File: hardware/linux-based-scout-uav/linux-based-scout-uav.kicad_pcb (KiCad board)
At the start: 2 copper layers, 60 x 90 mm, 39 parts, among them J1 XT60PW-M, J2 Micro_SD_Card_Det2, J3 TC2050-IDC-NL, J4 0786463001, J5 GSB1C41110SSHR, Q1 DMP3013SFV, Q2 DMP3013SFV, U1 OSD32MP157C-512M-IAA, U2 RN2903A-I_RM098, U3 M65, U4 LC76G, U5 MPU-6050, U6 AMG8833, U7 SX1272, U8 EMMC04G-W627-M06U, U9 CYPD3177-24LQ, Y1 ABS05-32.768KHZ-7-T

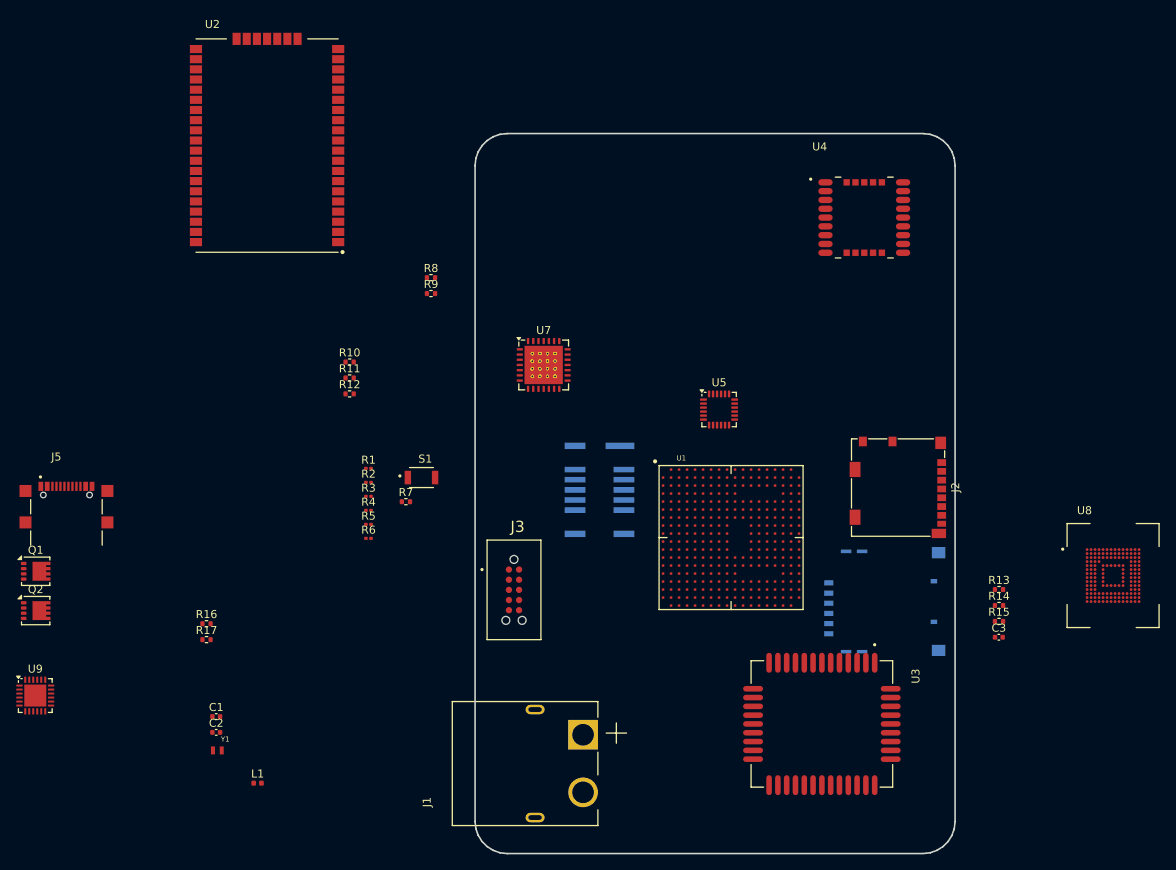
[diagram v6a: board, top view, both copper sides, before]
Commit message: Board placement update
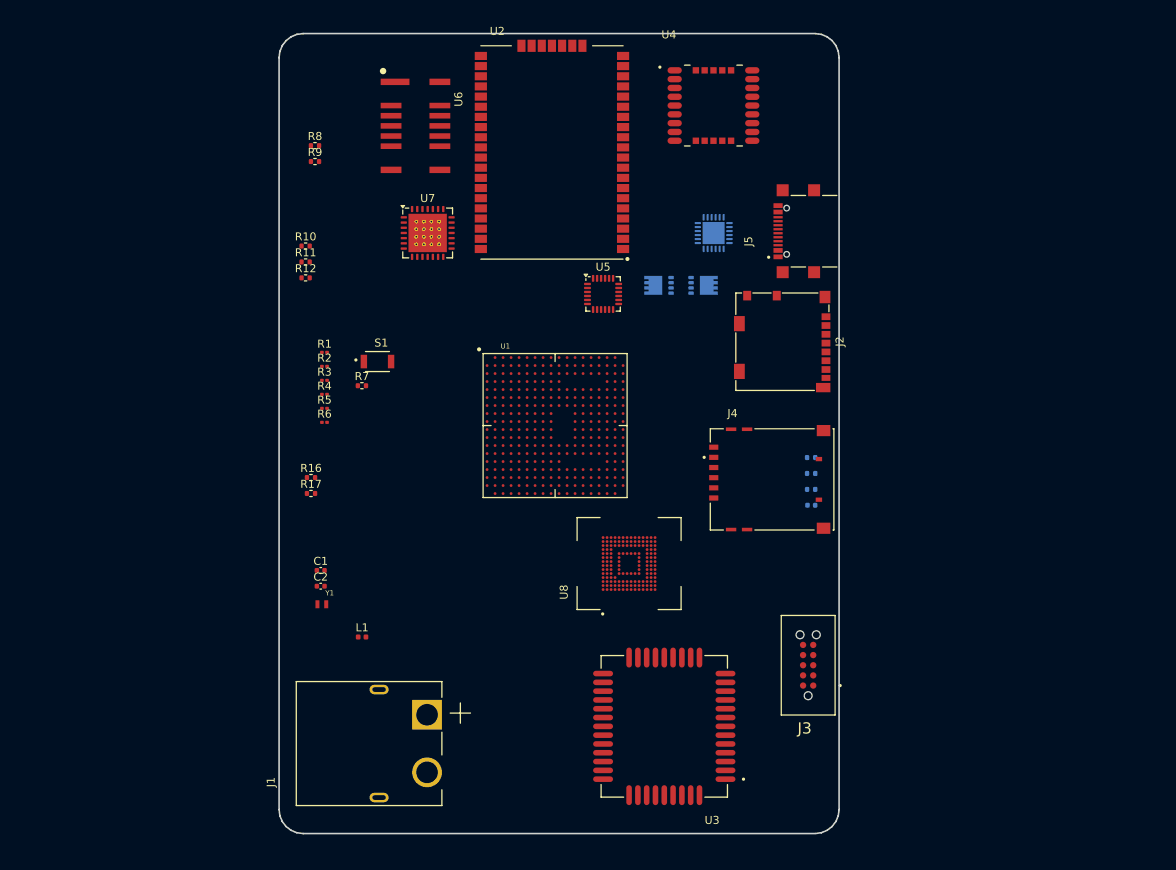
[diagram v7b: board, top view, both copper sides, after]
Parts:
- C3, Q1, Q2, R13, R14, R15, U9: moved to B.Cu
- J4, U6: moved to F.Cu
- moved U9 102.6 mm to (158.8, 74.9), turned to 180 degrees
- moved J5 99.2 mm to (170.6, 74.7), turned to 90 degrees
- moved Q1 90.8 mm to (157.5, 81.5)
- moved Q2 87.9 mm to (152.0, 81.5), turned to 180 degrees
- moved U8 60.5 mm to (148.2, 116.2), turned to 90 degrees
- moved U6 51.0 mm to (121.5, 61.5)
- moved J3 40.7 mm to (171.3, 131.5), turned to 180 degrees
- moved U2 35.6 mm to (138.6, 64.9)
- moved R13 28.7 mm to (171.0, 103.0), turned to 180 degrees
- moved R14 28.7 mm to (171.0, 105.0), turned to 180 degrees
- moved R15 28.7 mm to (171.0, 107.0), turned to 180 degrees
- moved C3 28.7 mm to (171.0, 109.0), turned to 180 degrees
- moved U1 26.1 mm to (139.0, 99.0)
- moved U4 23.5 mm to (158.8, 59.0)
- moved J2 23.3 mm to (167.4, 88.5)
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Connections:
- U1 pad D5: unconnected-(U1F-PWR_ON/PMIC_PWRCTRL-PadD5) -> Net-(U1F-PWR_ON/PMIC_PWRCTRL)
- U1 pad D6: unconnected-(U1F-PC13/PMIC_WAKEUP-PadD6) -> Net-(U1F-PC13/PMIC_WAKEUP)
- U1 pad J12: unconnected-(U1F-VTT_DDR-PadJ12) -> Net-(U1F-VTT_DDR)
- U1 pad J2: unconnected-(U1F-HSE_OSC_TP-PadJ2) -> Net-(U1F-HSE_OSC_TP)
- U1 pad K12: unconnected-(U1F-VDD_DDR-PadK12) -> Net-(U1F-VDD_DDR)
- U1 pad K6: unconnected-(U1F-PWR_LP-PadK6) -> Net-(U1F-PWR_LP)
- U1 pad L12: unconnected-(U1F-VREF_DDR-PadL12) -> Net-(U1F-VREF_DDR)
- U1 pad L3: unconnected-(U1F-PA0/PMIC_INTN-PadL3) -> Net-(U1F-PA0/PMIC_INTN)
- U1 pad L6: unconnected-(U1F-PDR_ON_CORE-PadL6) -> Net-(U1F-PDR_ON_CORE)
- U1 pad M6: unconnected-(U1F-PDR_ON-PadM6) -> Net-(U1F-PDR_ON)
- U1 pad N4: unconnected-(U1F-NRST_CORE-PadN4) -> Net-(U1F-NRST_CORE)
- U1 pad R4: unconnected-(U1F-VDD_CORE-PadR4) -> Net-(U1F-VDD_CORE)
- U1 pad R5: unconnected-(U1F-VDD3V3_USB-PadR5) -> Net-(U1F-VDD3V3_USB)
- U1 pad R6: unconnected-(U1F-VDD1V2_DSI_REG-PadR6) -> Net-(U1F-VDD1V2_DSI_REG)
- U1 pad R7: unconnected-(U1F-VDDA1V8_REG-PadR7) -> Net-(U1F-VDDA1V8_REG)
- U1 pad R8: unconnected-(U1F-VDDA1V1_REG-PadR8) -> Net-(U1F-VDDA1V1_REG)
- U1 pad T12: unconnected-(U1D-PE3-PadT12) -> MMC2_CLK
- U1 pad U15: unconnected-(U1D-PG6-PadU15) -> MMC2_CMD
- U8 pad A6: (no net) -> GND
- U8 pad A7: (no net) -> unconnected-(U8B-RFU_A7-PadA7)
- U8 pad C2: unconnected-(U8A-VDDI-PadC2) -> Net-(U8A-VDDI)
- U8 pad C4: (no net) -> GND
- U8 pad C6: (no net) -> +3V3
- U8 pad E10: GND -> unconnected-(U8A-VSF2-PadE10)
- U8 pad E5: (no net) -> unconnected-(U8B-RFU_E5-PadE5)
- U8 pad E6: (no net) -> +3V3
- U8 pad E7: (no net) -> GND
- U8 pad E8: GND -> unconnected-(U8A-VSF5-PadE8)
- U8 pad E9: GND -> unconnected-(U8A-VSF1-PadE9)
- U8 pad F10: GND -> unconnected-(U8A-VSF3-PadF10)
- U8 pad F5: (no net) -> +3V3
- U8 pad G10: GND -> unconnected-(U8A-VSF6-PadG10)
- U8 pad G3: (no net) -> unconnected-(U8B-RFU_G3-PadG3)
- U8 pad G5: (no net) -> GND
- U8 pad H1: (no net) -> Net-(U8B-NC_5-PadH1)
- U8 pad H10: (no net) -> GND
- U8 pad H12: (no net) -> Net-(U8B-NC_5-PadH1)
- U8 pad H13: (no net) -> Net-(U8B-NC_5-PadH1)
- U8 pad H14: (no net) -> Net-(U8B-NC_5-PadH1)
- U8 pad H2: (no net) -> Net-(U8B-NC_5-PadH1)
- U8 pad H3: (no net) -> Net-(U8B-NC_5-PadH1)
- U8 pad H5: unconnected-(U8A-DS-PadH5) -> Net-(U8A-DS)
- U8 pad J1: (no net) -> Net-(U8B-NC_5-PadH1)
- U8 pad J10: (no net) -> +3V3
- U8 pad J12: (no net) -> Net-(U8B-NC_5-PadH1)
- U8 pad J13: (no net) -> Net-(U8B-NC_5-PadH1)
- U8 pad J14: (no net) -> Net-(U8B-NC_5-PadH1)
- U8 pad J2: (no net) -> Net-(U8B-NC_5-PadH1)
- U8 pad J3: (no net) -> Net-(U8B-NC_5-PadH1)
- U8 pad J5: (no net) -> GND
- U8 pad K1: (no net) -> Net-(U8B-NC_5-PadH1)
- U8 pad K10: GND -> unconnected-(U8A-VSF4-PadK10)
- U8 pad K12: (no net) -> Net-(U8B-NC_6-PadK12)
- U8 pad K13: (no net) -> Net-(U8B-NC_6-PadK12)
- U8 pad K14: (no net) -> Net-(U8B-NC_6-PadK12)
- U8 pad K2: (no net) -> Net-(U8B-NC_5-PadH1)
- U8 pad K3: (no net) -> Net-(U8B-NC_5-PadH1)
- U8 pad K5: unconnected-(U8A-~{RST}-PadK5) -> NRST
- U8 pad K6: (no net) -> unconnected-(U8B-RFU_K6-PadK6)
- U8 pad K7: (no net) -> unconnected-(U8B-RFU_K7-PadK7)
- U8 pad K8: (no net) -> GND
- U8 pad K9: (no net) -> +3V3
- U8 pad L1: (no net) -> Net-(U8B-NC_6-PadK12)
- U8 pad L12: (no net) -> Net-(U8B-NC_6-PadK12)
- U8 pad L13: (no net) -> Net-(U8B-NC_6-PadK12)
- U8 pad L14: (no net) -> Net-(U8B-NC_6-PadK12)
- U8 pad L2: (no net) -> Net-(U8B-NC_6-PadK12)
- U8 pad L3: (no net) -> Net-(U8B-NC_6-PadK12)
- U8 pad M1: (no net) -> Net-(U8B-NC_6-PadK12)
- U8 pad M10: (no net) -> Net-(U8B-NC_7-PadM10)
- U8 pad M11: (no net) -> Net-(U8B-NC_7-PadM10)
- U8 pad M12: (no net) -> Net-(U8B-NC_7-PadM10)
- U8 pad M13: (no net) -> Net-(U8B-NC_7-PadM10)
- U8 pad M14: (no net) -> Net-(U8B-NC_7-PadM10)
- U8 pad M2: (no net) -> Net-(U8B-NC_6-PadK12)
- U8 pad M3: (no net) -> Net-(U8B-NC_6-PadK12)
- U8 pad M4: (no net) -> +3V3
- U8 pad M5: unconnected-(U8A-CMD-PadM5) -> MMC2_CMD
- U8 pad M6: unconnected-(U8A-CLK-PadM6) -> MMC2_CLK
- U8 pad M7: (no net) -> Net-(U8B-NC_6-PadK12)
- U8 pad M8: (no net) -> Net-(U8B-NC_7-PadM10)
- U8 pad M9: (no net) -> Net-(U8B-NC_7-PadM10)
- U8 pad N1: (no net) -> Net-(U8B-NC_7-PadM10)
- U8 pad N10: (no net) -> Net-(U8B-NC_7-PadM10)
- U8 pad N11: (no net) -> Net-(U8B-NC_8-PadN11)
- U8 pad N12: (no net) -> Net-(U8B-NC_8-PadN11)
- U8 pad N13: (no net) -> Net-(U8B-NC_8-PadN11)
- U8 pad N14: (no net) -> Net-(U8B-NC_8-PadN11)
- U8 pad N2: (no net) -> GND
- U8 pad N3: (no net) -> Net-(U8B-NC_7-PadM10)
- U8 pad N4: (no net) -> +3V3
- U8 pad N5: (no net) -> GND
- U8 pad N6: (no net) -> Net-(U8B-NC_7-PadM10)
- U8 pad N7: (no net) -> Net-(U8B-NC_7-PadM10)
- U8 pad N8: (no net) -> Net-(U8B-NC_7-PadM10)
- U8 pad N9: (no net) -> Net-(U8B-NC_7-PadM10)
- U8 pad P1: (no net) -> Net-(U8B-NC_8-PadN11)
- U8 pad P10: (no net) -> unconnected-(U8B-RFU_P10-PadP10)
- U8 pad P11: (no net) -> Net-(U8B-NC_8-PadN11)
- U8 pad P12: (no net) -> Net-(U8B-NC_8-PadN11)
- U8 pad P13: (no net) -> Net-(U8B-NC_8-PadN11)
- U8 pad P14: (no net) -> Net-(U8B-NC_8-PadN11)
- U8 pad P2: (no net) -> Net-(U8B-NC_8-PadN11)
- U8 pad P3: (no net) -> +3V3
- U8 pad P4: (no net) -> GND
- U8 pad P5: (no net) -> +3V3
- U8 pad P6: (no net) -> GND
- U8 pad P7: (no net) -> unconnected-(U8B-RFU_P7-PadP7)
- U8 pad P8: (no net) -> Net-(U8B-NC_8-PadN11)
- U8 pad P9: (no net) -> Net-(U8B-NC_8-PadN11)
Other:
- board size 60 x 90 mm -> 70 x 100 mm

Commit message: Schematic and board update
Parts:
- added U10: G313-06329-00, G313-06329-00:MODULE_G313-06329-00, F.Cu at (133.6, 119.5)
- moved J3 5.15 mm to (171.3, 126.3)
- moved J1 2.93 mm to (116.0, 136.0), turned to 180 degrees
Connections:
- net USB_DP1 renamed USB_DP
- J5 pad A7: USB_DM1 -> USB_DM
- J5 pad B6: USB_DP2 -> unconnected-(J5-DP2-PadB6)
- J5 pad B7: USB_DM2 -> unconnected-(J5-DN2-PadB7)
- U1 pad J17: USB_DM2 -> USB_2_DN
- U1 pad J18: USB_DP2 -> USB_2_DP
- U1 pad K18: USB_DM1 -> USB_DN
